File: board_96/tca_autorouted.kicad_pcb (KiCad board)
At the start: 2 copper layers, 143 x 74 mm, 170 parts, among them IC1 ATMEGA328-A, P1 CONN_2, P2 CONN_3X2, Q1 BSS138, U1 SD_CARD, U10 TLC5941, U11 TLC5941, U12 TLC5941, U13 TLC5941, U14 TLC5941, U15 TLC5941, U2 LD1117S50, U3 LD1117S33, U4 TLC5941, U5 TLC5941, U6 TLC5941, U7 TLC5941, U8 TLC5941, U9 TLC5941, Y1 RESONATEUR

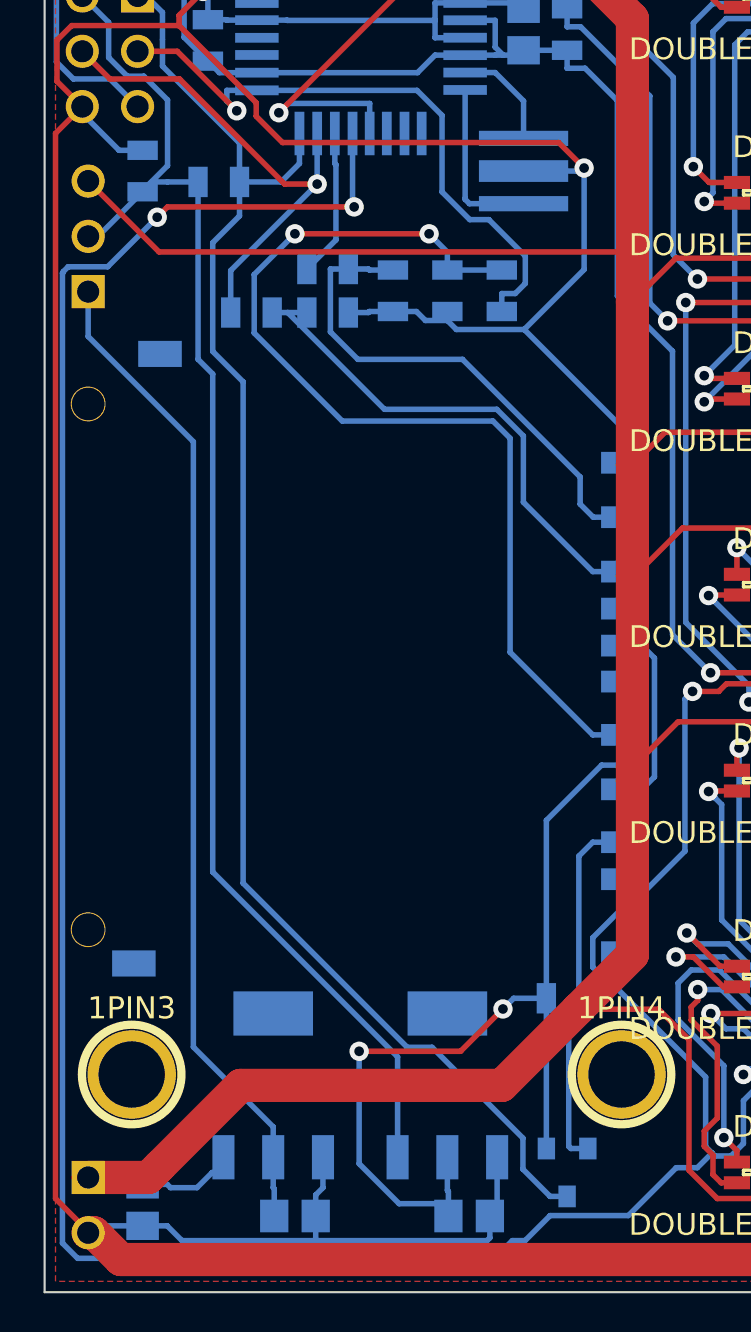
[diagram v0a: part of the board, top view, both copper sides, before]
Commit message: small gnd updates
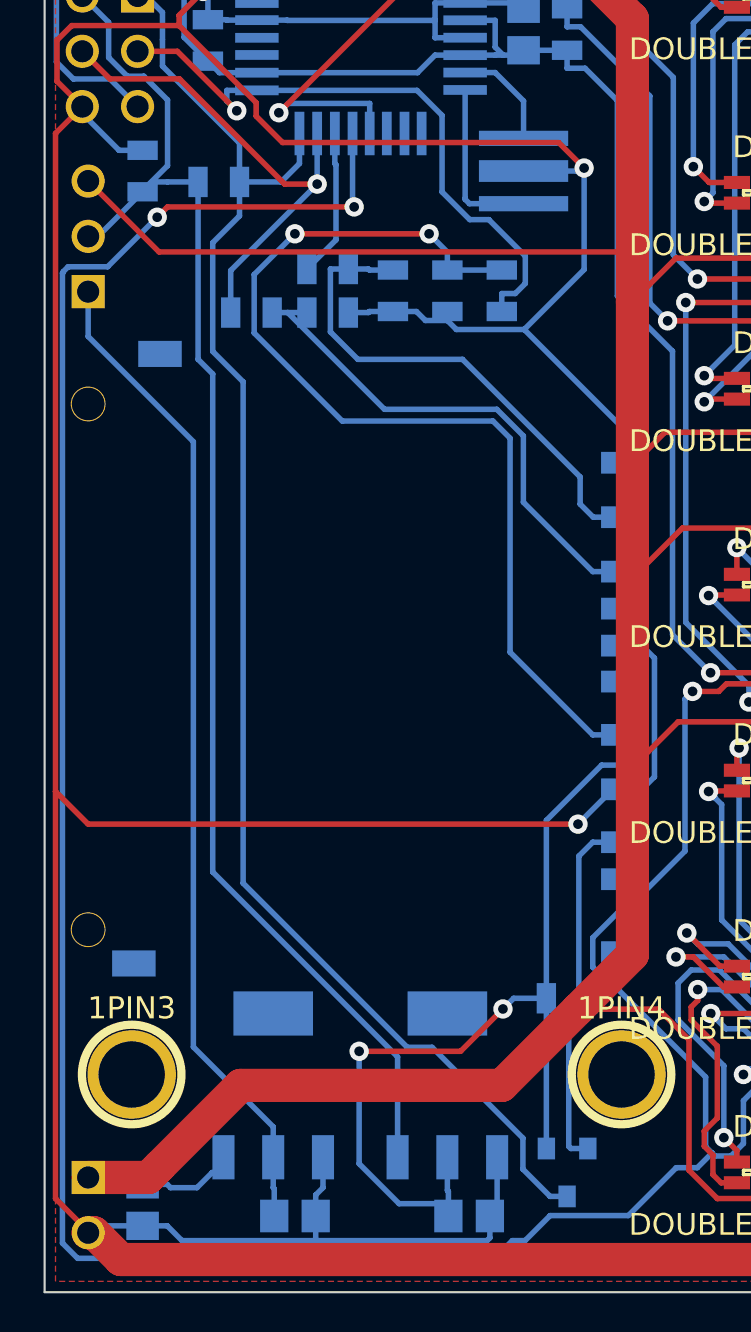
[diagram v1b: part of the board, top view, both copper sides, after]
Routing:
- net GND: track 654.5 -> 681.6 mm, vias 15 -> 16
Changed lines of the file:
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@@
     (thickness 1.6)
     (drawings 108)
-    (tracks 4410)
+    (tracks 4416)
     (zones 0)
     (modules 170)
@@
   (segment (start 82.4995 102.452) (end 82.5 102.4525) (width 0.254) (layer B.Cu) (net 1))
   (segment (start 84.3 103.278) (end 85.1745 103.278) (width 0.254) (layer B.Cu) (net 2))
-  (segment (start 85.1745 103.278) (end 86 102.4525) (width 0.254) (layer B.Cu) (net 2) (status 800000))
+  (segment (start 85.1745 103.278) (end 86 102.4525) (width 0.254) (layer B.Cu) (net 2))
   (segment (start 86 102.452) (end 86 102.4525) (width 0.254) (layer B.Cu) (net 2))
   (segment (start 81.1241 104.293) (end 81.1241 105.674) (width 0.254) (layer B.Cu) (net 2))
   (segment (start 82.139 103.278) (end 81.1241 104.293) (width 0.254) (layer B.Cu) (net 2))
   (segment (start 84.3 103.278) (end 82.139 103.278) (width 0.254) (layer B.Cu) (net 2))
-  (segment (start 71.27 108.96) (end 71.66 108.96) (width 0.254) (layer B.Cu) (net 3) (status C00000))
+  (segment (start 71.27 108.96) (end 71.66 108.96) (width 0.254) (layer B.Cu) (net 3))
   (segment (start 72.4133 109.7133) (end 72.4133 110.9607) (width 0.254) (layer B.Cu) (net 3))
-  (segment (start 71.66 108.96) (end 72.4133 109.7133) (width 0.254) (layer B.Cu) (net 3) (status 400000))
+  (segment (start 71.66 108.96) (end 72.4133 109.7133) (width 0.254) (layer B.Cu) (net 3))
   (segment (start 78.706 115.9656) (end 78.706 116.656) (width 0.254) (layer B.Cu) (net 3))
   (segment (start 78.706 115.9656) (end 78.706 115.2752) (width 0.254) (layer B.Cu) (net 3))
@@
   (segment (start 79 102.4525) (end 79 103.278) (width 0.254) (layer B.Cu) (net 5))
   (segment (start 79 102.452) (end 79 102.4525) (width 0.254) (layer B.Cu) (net 5))
-  (segment (start 76.475 100.25) (end 76.475 105.1983) (width 0.254) (layer B.Cu) (net 6) (status 400000))
+  (segment (start 76.475 100.25) (end 76.475 105.1983) (width 0.254) (layer B.Cu) (net 6))
   (segment (start 76.475 105.1983) (end 76.7767 105.5) (width 0.254) (layer B.Cu) (net 6))
   (segment (start 76.475 100.25) (end 76.475 101.0725) (width 0.254) (layer B.Cu) (net 6))
@@
   (segment (start 200.2 105.7) (end 199.9 105.4) (width 0.254) (layer B.Cu) (net 18))
   (segment (start 197.5562 105.4) (end 197.556 105.3998) (width 0.254) (layer B.Cu) (net 18))
-  (segment (start 71.5 117.9525) (end 71.5 117.9) (width 0.254) (layer B.Cu) (net 19) (status C00000))
-  (segment (start 71.5 117.9) (end 72.6464 116.7536) (width 0.254) (layer B.Cu) (net 19) (status 400000))
-  (segment (start 74.0475 117.5) (end 74.0475 125.6475) (width 0.254) (layer B.Cu) (net 19) (status 400000))
+  (segment (start 71.5 117.9525) (end 71.5 117.9) (width 0.254) (layer B.Cu) (net 19))
+  (segment (start 71.5 117.9) (end 72.6464 116.7536) (width 0.254) (layer B.Cu) (net 19))
+  (segment (start 74.0475 117.5) (end 74.0475 125.6475) (width 0.254) (layer B.Cu) (net 19))
   (segment (start 74.0475 125.6475) (end 74.7216 126.3216) (width 0.254) (layer B.Cu) (net 19))
-  (segment (start 69 120) (end 69.4525 120) (width 0.254) (layer B.Cu) (net 19) (status C00000))
-  (segment (start 69.4525 120) (end 71.5 117.9525) (width 0.254) (layer B.Cu) (net 19) (status C00000))
+  (segment (start 69 120) (end 69.4525 120) (width 0.254) (layer B.Cu) (net 19))
+  (segment (start 69.4525 120) (end 71.5 117.9525) (width 0.254) (layer B.Cu) (net 19))
   (segment (start 87.6966 110.076) (end 87.6966 111.3088) (width 0.254) (layer B.Cu) (net 19))
   (segment (start 86.316 110.076) (end 87.6966 110.076) (width 0.254) (layer B.Cu) (net 19))
@@
   (segment (start 87.0062 111.676) (end 86.3158 111.676) (width 0.254) (layer B.Cu) (net 19))
   (segment (start 87.0062 111.676) (end 87.6966 111.676) (width 0.254) (layer B.Cu) (net 19))
-  (segment (start 88.0638 111.676) (end 88.7765 111.676) (width 0.254) (layer B.Cu) (net 19) (status 800000))
-  (segment (start 88.7765 111.676) (end 89 111.4525) (width 0.254) (layer B.Cu) (net 19) (status C00000))
+  (segment (start 88.0638 111.676) (end 88.7765 111.676) (width 0.254) (layer B.Cu) (net 19))
+  (segment (start 88.7765 111.676) (end 89 111.4525) (width 0.254) (layer B.Cu) (net 19))
   (via (at 150.429 158.145) (size 0.889) (layers F.Cu B.Cu) (net 19))
   (via (at 149.507 151.199) (size 0.889) (layers F.Cu B.Cu) (net 19))
@@
   (segment (start 100.4438 105.4) (end 101.46 105.4) (width 0.254) (layer B.Cu) (net 22))
   (segment (start 101.4442 157.6) (end 101.444 157.6002) (width 0.254) (layer B.Cu) (net 22))
-  (segment (start 69 165.77) (end 69 165.7) (width 0.254) (layer F.Cu) (net 23) (status C00000))
-  (segment (start 67.5 115.27) (end 68.73 114.04) (width 0.254) (layer F.Cu) (net 23) (status 800000))
-  (segment (start 67.5 164.2) (end 67.5 115.27) (width 0.254) (layer F.Cu) (net 23))
-  (segment (start 69 165.7) (end 67.5 164.2) (width 0.254) (layer F.Cu) (net 23) (status 400000))
-  (segment (start 194.0475 164.5) (end 193.5 164.5) (width 0.254) (layer B.Cu) (net 23) (status 400000))
+  (segment (start 69 147) (end 67.5 145.5) (width 0.254) (layer F.Cu) (net 23))
+  (segment (start 91.5 147) (end 69 147) (width 0.254) (layer F.Cu) (net 23))
+  (via (at 91.5 147) (size 0.889) (layers F.Cu B.Cu) (net 23))
+  (segment (start 93.1 145.4) (end 91.5 147) (width 0.254) (layer B.Cu) (net 23))
+  (segment (start 93.31 145.4) (end 93.1 145.4) (width 0.254) (layer B.Cu) (net 23))
+  (segment (start 67.5 145.5) (end 67.5 115.27) (width 0.254) (layer F.Cu) (net 23))
+  (segment (start 69 165.77) (end 69 165.7) (width 0.254) (layer F.Cu) (net 23))
+  (segment (start 69 165.7) (end 67.5 164.2) (width 0.254) (layer F.Cu) (net 23))
+  (segment (start 67.5 164.2) (end 67.5 145.5) (width 0.254) (layer F.Cu) (net 23))
+  (segment (start 67.5 115.27) (end 68.73 114.04) (width 0.254) (layer F.Cu) (net 23))
+  (segment (start 194.0475 164.5) (end 193.5 164.5) (width 0.254) (layer B.Cu) (net 23))
   (segment (start 192.5 165.5) (end 192.5 167) (width 0.254) (layer F.Cu) (net 23))
   (via (at 192.5 165.5) (size 0.889) (layers F.Cu B.Cu) (net 23))
   (segment (start 193.5 164.5) (end 192.5 165.5) (width 0.254) (layer B.Cu) (net 23))
-  (segment (start 176.0475 164.5) (end 175.4 164.5) (width 0.254) (layer B.Cu) (net 23) (status 400000))
+  (segment (start 176.0475 164.5) (end 175.4 164.5) (width 0.254) (layer B.Cu) (net 23))
   (segment (start 174.4 165.5) (end 174.4 167) (width 0.254) (layer F.Cu) (net 23))
   (via (at 174.4 165.5) (size 0.889) (layers F.Cu B.Cu) (net 23))
   (segment (start 175.4 164.5) (end 174.4 165.5) (width 0.254) (layer B.Cu) (net 23))
-  (segment (start 158.0475 164.5) (end 157.5 164.5) (width 0.254) (layer B.Cu) (net 23) (status 400000))
+  (segment (start 158.0475 164.5) (end 157.5 164.5) (width 0.254) (layer B.Cu) (net 23))
   (segment (start 156.5 165.5) (end 156.5 167) (width 0.254) (layer F.Cu) (net 23))
   (via (at 156.5 165.5) (size 0.889) (layers F.Cu B.Cu) (net 23))
   (segment (start 157.5 164.5) (end 156.5 165.5) (width 0.254) (layer B.Cu) (net 23))
-  (segment (start 140.0475 164.5) (end 139.6 164.5) (width 0.254) (layer B.Cu) (net 23) (status 400000))
+  (segment (start 140.0475 164.5) (end 139.6 164.5) (width 0.254) (layer B.Cu) (net 23))
   (segment (start 138.6 165.5) (end 138.6 167) (width 0.254) (layer F.Cu) (net 23))
   (via (at 138.6 165.5) (size 0.889) (layers F.Cu B.Cu) (net 23))
   (segment (start 139.6 164.5) (end 138.6 165.5) (width 0.254) (layer B.Cu) (net 23))
-  (segment (start 122.0475 164.5) (end 121.5 164.5) (width 0.254) (layer B.Cu) (net 23) (status 400000))
+  (segment (start 122.0475 164.5) (end 121.5 164.5) (width 0.254) (layer B.Cu) (net 23))
   (segment (start 120.5 165.5) (end 120.5 167) (width 0.254) (layer F.Cu) (net 23))
   (segment (start 120.6 165.4) (end 120.5 165.5) (width 0.254) (layer F.Cu) (net 23))
   (via (at 120.6 165.4) (size 0.889) (layers F.Cu B.Cu) (net 23))
   (segment (start 121.5 164.5) (end 120.6 165.4) (width 0.254) (layer B.Cu) (net 23))
-  (segment (start 104.0475 164.5) (end 103.4 164.5) (width 0.254) (layer B.Cu) (net 23) (status 400000))
+  (segment (start 104.0475 164.5) (end 103.4 164.5) (width 0.254) (layer B.Cu) (net 23))
   (segment (start 102.6 165.3) (end 102.6 167) (width 0.254) (layer F.Cu) (net 23))
   (via (at 102.6 165.3) (size 0.889) (layers F.Cu B.Cu) (net 23))
   (segment (start 103.4 164.5) (end 102.6 165.3) (width 0.254) (layer B.Cu) (net 23))
-  (segment (start 79.4525 165) (end 79.4525 164.0325) (width 0.254) (layer B.Cu) (net 23) (status 400000))
+  (segment (start 79.4525 165) (end 79.4525 164.0325) (width 0.254) (layer B.Cu) (net 23))
   (segment (start 79.4525 164.0325) (end 79.786 163.699) (width 0.254) (layer B.Cu) (net 23))
   (via (at 195 96.5) (size 0.889) (layers F.Cu B.Cu) (net 23))
@@
   (segment (start 173.4436 153.689) (end 173.444 153.6886) (width 0.254) (layer B.Cu) (net 80))
   (segment (start 86.31584 118.24714) (end 86.31584 118.299816) (width 0.254) (layer B.Cu) (net 81))
-  (segment (start 86.31584 113.27622) (end 86.31584 118.24714) (width 0.254) (layer B.Cu) (net 81) (status 400000))
-  (segment (start 86.516024 118.5) (end 89 118.5) (width 0.254) (layer B.Cu) (net 81) (status 800000))
+  (segment (start 86.31584 113.27622) (end 86.31584 118.24714) (width 0.254) (layer B.Cu) (net 81))
+  (segment (start 86.516024 118.5) (end 89 118.5) (width 0.254) (layer B.Cu) (net 81))
   (segment (start 86.31584 118.299816) (end 86.516024 118.5) (width 0.254) (layer B.Cu) (net 81))
   (segment (start 86.3158 113.276) (end 86.316 113.276) (width 0.254) (layer B.Cu) (net 81))

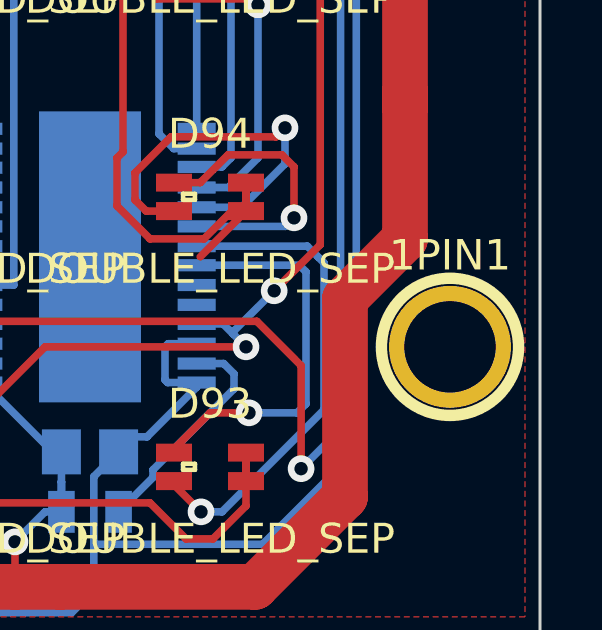
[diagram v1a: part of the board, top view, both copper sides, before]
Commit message: Move a mounting pin
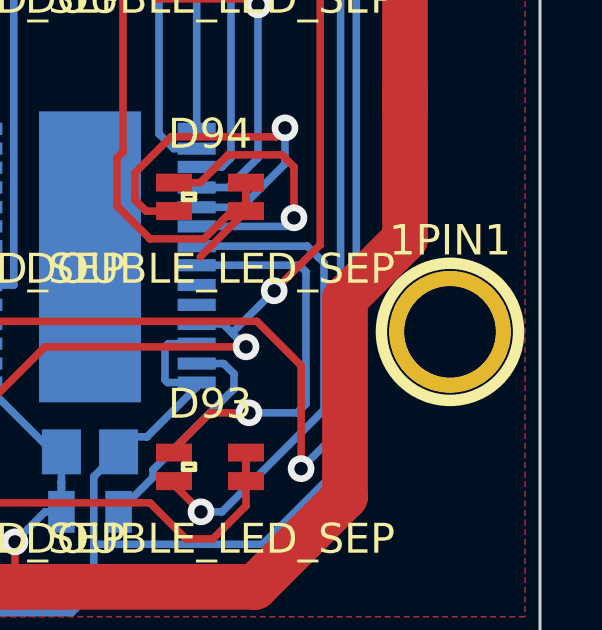
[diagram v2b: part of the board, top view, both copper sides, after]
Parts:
- moved 1PIN1 0.50 mm to (207.0, 158.5)
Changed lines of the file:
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@@
   )
   (module 1pin (layer F.Cu)
-    (at 207 159)
+    (at 207 158.5)
     (descr "module 1 pin (ou trou mecanique de percage)")
     (tags DEV)

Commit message: Design which was submitted to OSHpark
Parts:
- P1: footprint PIN_ARRAY_2X1 -> PIN_ARRAY_2X1_3960um
- moved C3 3.70 mm to (75.0, 165.7)
- moved P1 2.91 mm to (71.9, 164.7)
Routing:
- net GND: track 681.6 -> 676.8 mm, vias 16 -> 17
- net /tlcs_1-6/VIN: track 1475.8 -> 1471.8 mm
- net /tlcs_1-6/SCLK: track 522.4 -> 520.6 mm
- net /tlcs_1-6/XLAT: track 522.2 -> 521.2 mm
